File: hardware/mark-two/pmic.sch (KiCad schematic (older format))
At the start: 30 parts, among them U1 MC34PF1510A6EP

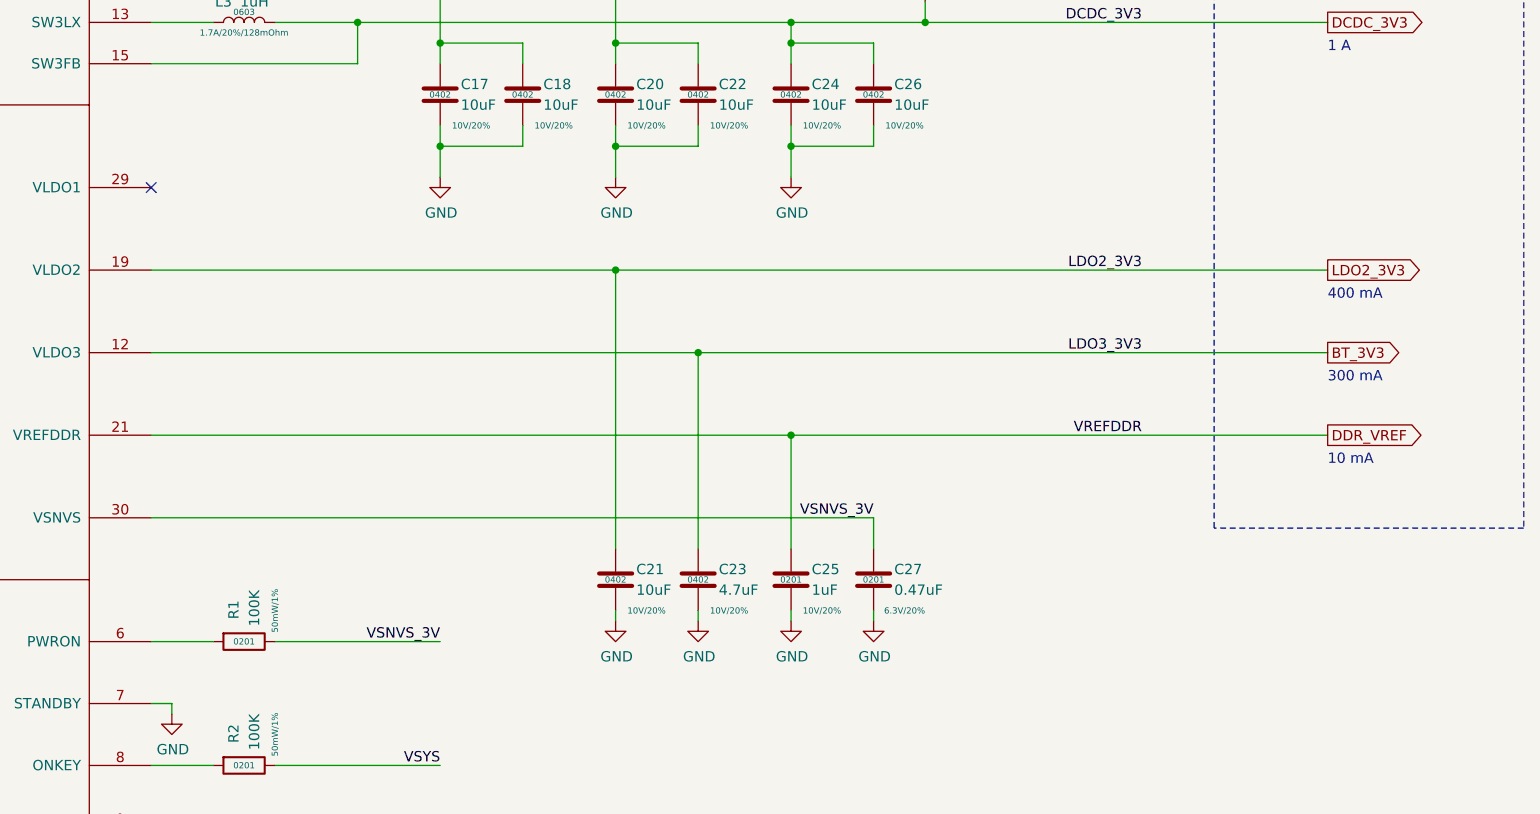
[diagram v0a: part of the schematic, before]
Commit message: add USB armory Mk II rev. γ
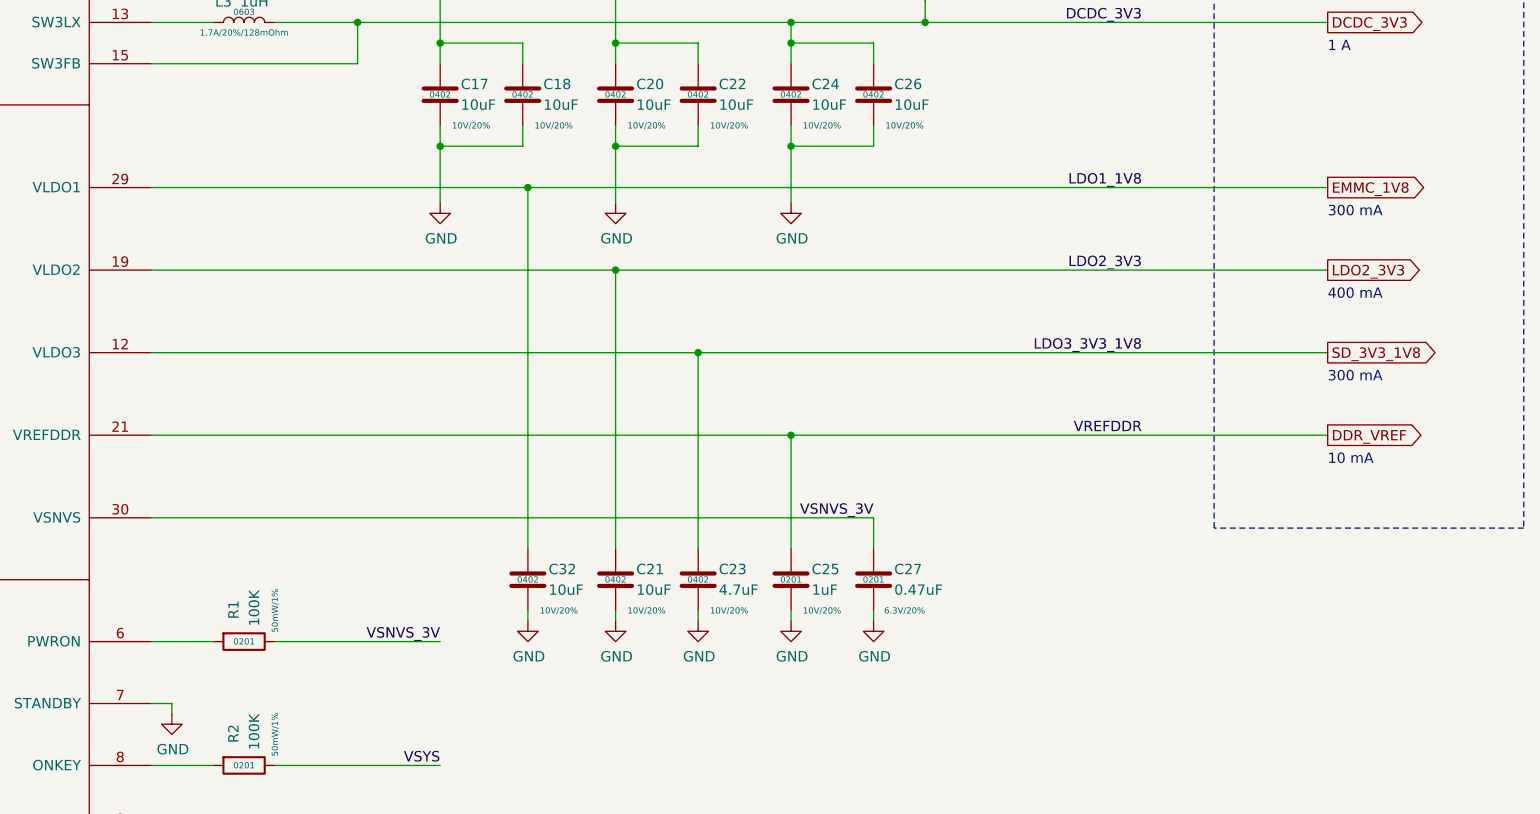
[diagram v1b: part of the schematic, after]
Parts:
- added C32: 10uF, armory-kicad:SM0402, symbol Device:C
- C10, C14, C15, C25, C4, C8, C9: Alternative PN (none) -> CL03A105KP3NSNC
- C13: Alternative PN (none) -> GRT155R61E225KE13D
- C16: Alternative PN (none) -> 06036D476MAT2A
- U1: Alternative PN (none) -> MC32PF1510A6EP
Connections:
- net GND: now also C32.2
- net EMMC_1V8: now reaches U1.29 (VLDO1)
- net EMMC_1V8: now also C32.1
- net BT_3V3 renamed SD_3V3_1V8
- no-connect marks 7 -> 6
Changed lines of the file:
@@
 EESchema Schematic File Version 4
-LIBS:armory-cache
 EELAYER 30 0
 EELAYER END
@@
 encoding utf-8
 Sheet 13 13
-Title "USB ARMORY"
-Date "2019-06-25"
-Rev "MARK II"
+Title "USB armory Mk II"
+Date "2021-02-18"
+Rev "γ"
 Comp "F-Secure"
-Comment1 "Copyright © 2019 F-Secure"
-Comment2 "License: CERN OHL v1.2"
-Comment3 "https://github.com/inversepath/usbarmory"
+Comment1 "Copyright © F-Secure Corporation"
+Comment2 "License: CERN-OHL-S"
+Comment3 "https://github.com/f-secure-foundry/usbarmory"
 Comment4 ""
 $EndDescr
@@
 LDO2_3V3
 Text Label 13150 5000 2    50   ~ 0
-LDO3_3V3
+LDO3_3V3_1V8
 $Comp
 L power:GND #PWR?
@@
 L power:GND #PWR?
 U 1 1 5C23D7E7
-P 9750 4150
+P 9750 4275
 AR Path="/5BEA6694/5C23D7E7" Ref="#PWR?"  Part="1"
 AR Path="/53722D05/5C23D7E7" Ref="#PWR?"  Part="1"
@@
 AR Path="/5C6BBC6A/5C23D7E7" Ref="#PWR?"  Part="1"
 AR Path="/5D0EEC79/5C23D7E7" Ref="#PWR?"  Part="1"
-F 0 "#PWR016" H 9750 3900 50  0001 C CNN
-F 1 "GND" H 9755 3977 50  0000 C CNN
-F 2 "" H 9750 4150 50  0001 C CNN
-F 3 "" H 9750 4150 50  0001 C CNN
-	1    9750 4150
+F 0 "#PWR016" H 9750 4025 50  0001 C CNN
+F 1 "GND" H 9755 4102 50  0000 C CNN
+F 2 "" H 9750 4275 50  0001 C CNN
+F 3 "" H 9750 4275 50  0001 C CNN
+	1    9750 4275
 	1    0    0    -1
 $EndComp
@@
 Connection ~ 9750 4000
 Wire Wire Line
-	9750 4000 9750 4150
+	9750 4000 9750 4275
 $Comp
 L power:GND #PWR?
 U 1 1 5C2BD78A
-P 10600 4150
+P 10600 4275
 AR Path="/5BEA6694/5C2BD78A" Ref="#PWR?"  Part="1"
 AR Path="/53722D05/5C2BD78A" Ref="#PWR?"  Part="1"
@@
 AR Path="/5C6BBC6A/5C2BD78A" Ref="#PWR?"  Part="1"
 AR Path="/5D0EEC79/5C2BD78A" Ref="#PWR?"  Part="1"
-F 0 "#PWR018" H 10600 3900 50  0001 C CNN
-F 1 "GND" H 10605 3977 50  0000 C CNN
-F 2 "" H 10600 4150 50  0001 C CNN
-F 3 "" H 10600 4150 50  0001 C CNN
-	1    10600 4150
+F 0 "#PWR018" H 10600 4025 50  0001 C CNN
+F 1 "GND" H 10605 4102 50  0000 C CNN
+F 2 "" H 10600 4275 50  0001 C CNN
+F 3 "" H 10600 4275 50  0001 C CNN
+	1    10600 4275
 	1    0    0    -1
 $EndComp
@@
 Connection ~ 10600 4000
 Wire Wire Line
-	10600 4000 10600 4150
+	10600 4000 10600 4275
 Wire Wire Line
 	10600 3600 10600 3500
@@
 L power:GND #PWR?
 U 1 1 5C2FA4BD
-P 11450 4150
+P 11450 4275
 AR Path="/5BEA6694/5C2FA4BD" Ref="#PWR?"  Part="1"
 AR Path="/53722D05/5C2FA4BD" Ref="#PWR?"  Part="1"
@@
 AR Path="/5C6BBC6A/5C2FA4BD" Ref="#PWR?"  Part="1"
 AR Path="/5D0EEC79/5C2FA4BD" Ref="#PWR?"  Part="1"
-F 0 "#PWR021" H 11450 3900 50  0001 C CNN
-F 1 "GND" H 11455 3977 50  0000 C CNN
-F 2 "" H 11450 4150 50  0001 C CNN
-F 3 "" H 11450 4150 50  0001 C CNN
-	1    11450 4150
+F 0 "#PWR021" H 11450 4025 50  0001 C CNN
+F 1 "GND" H 11455 4102 50  0000 C CNN
+F 2 "" H 11450 4275 50  0001 C CNN
+F 3 "" H 11450 4275 50  0001 C CNN
+	1    11450 4275
 	1    0    0    -1
 $EndComp
@@
 Connection ~ 11450 4000
 Wire Wire Line
-	11450 4000 11450 4150
+	11450 4000 11450 4275
 Wire Wire Line
 	11450 3600 11450 3500
@@
 LDO2_3V3
 Text GLabel 14050 5000 2    50   Output ~ 0
-BT_3V3
+SD_3V3_1V8
 Text GLabel 4550 7200 0    50   Input ~ 0
 I2C1_SCL
@@
 F 7 "Digikey" H 7100 1000 50  0001 C CNN "Supplier"
 F 8 "568-14653-1-ND" H 7100 1000 50  0001 C CNN "Supplier PN"
+F 9 "MC32PF1510A6EP" H 7100 1000 50  0001 C CNN "Alternative PN"
 	1    7100 1000
 	1    0    0    -1
@@
 Wire Wire Line
 	11000 5000 11000 5950
-NoConn ~ 8350 4200
 Text Label 9750 7000 2    50   ~ 0
 VSYS
@@
 Text Label 9750 6400 2    50   ~ 0
 VSNVS_3V
-Wire Wire Line
-	10600 5950 10600 4600
 Wire Wire Line
 	8350 4600 10600 4600
@@
 F 9 "0201" H 1900 4550 30  0000 C CNN "FP"
 F 10 "10V/20%" H 2050 4400 30  0000 C CNN "Rating"
+F 11 "CL03A105KP3NSNC" H 1900 4550 50  0001 C CNN "Alternative PN"
 	1    1900 4550
 	1    0    0    -1
@@
 F 9 "0201" H 2350 4550 30  0000 C CNN "FP"
 F 10 "10V/20%" H 2500 4400 30  0000 C CNN "Rating"
+F 11 "CL03A105KP3NSNC" H 2350 4550 50  0001 C CNN "Alternative PN"
 	1    2350 4550
 	1    0    0    -1
@@
 F 9 "0201" H 2800 4550 30  0000 C CNN "FP"
 F 10 "10V/20%" H 2950 4400 30  0000 C CNN "Rating"
+F 11 "CL03A105KP3NSNC" H 2800 4550 50  0001 C CNN "Alternative PN"
 	1    2800 4550
 	1    0    0    -1
@@
 F 9 "0201" H 5200 9050 30  0000 C CNN "FP"
 F 10 "10V/20%" H 5350 8900 30  0000 C CNN "Rating"
+F 11 "CL03A105KP3NSNC" H 5200 9050 50  0001 C CNN "Alternative PN"
 	1    5200 9050
 	1    0    0    -1
@@
 F 9 "0201" H 5650 9050 30  0000 C CNN "FP"
 F 10 "10V/20%" H 5800 8900 30  0000 C CNN "Rating"
+F 11 "CL03A105KP3NSNC" H 5650 9050 50  0001 C CNN "Alternative PN"
 	1    5650 9050
 	1    0    0    -1
@@
 F 9 "0201" H 11450 6100 30  0000 C CNN "FP"
 F 10 "10V/20%" H 11600 5950 30  0000 C CNN "Rating"
+F 11 "CL03A105KP3NSNC" H 11450 6100 50  0001 C CNN "Alternative PN"
 	1    11450 6100
 	1    0    0    -1
@@
 F 9 "0402" H 5200 1450 30  0000 C CNN "FP"
 F 10 "25V/20%" H 5350 1300 30  0000 C CNN "Rating"
+F 11 "GRT155R61E225KE13D" H 5200 1450 50  0001 C CNN "Alternative PN"
 	1    5200 1450
 	1    0    0    -1
@@
 F 9 "0603" H 9750 1450 30  0000 C CNN "FP"
 F 10 "6.3V/20%" H 9900 1300 30  0000 C CNN "Rating"
+F 11 "06036D476MAT2A" H 9750 1450 50  0001 C CNN "Alternative PN"
 	1    9750 1450
 	1    0    0    -1
@@
 F 9 "0201" H 4250 6000 30  0000 C CNN "FP"
 F 10 "10V/20%" H 4400 5850 30  0000 C CNN "Rating"
+F 11 "CL03A105KP3NSNC" H 4250 6000 50  0001 C CNN "Alternative PN"
 	1    4250 6000
 	1    0    0    -1
@@
 Text Notes 5725 10000 0    100  ~ 0
 ULL/ULZ: NXP MC34PF1510A6EP\n      UL: NXP MC32PF1510A3EP
+Wire Wire Line
+	10600 5950 10600 4600
+Text GLabel 14050 4200 2    50   Output ~ 0
+EMMC_1V8
+Text Notes 14050 4350 0    50   ~ 0
+300 mA
+$Comp
+L power:GND #PWR?
+U 1 1 5F1896E1
+P 10175 6300
+AR Path="/5BEA6694/5F1896E1" Ref="#PWR?"  Part="1"
+AR Path="/53722D05/5F1896E1" Ref="#PWR?"  Part="1"
+AR Path="/5335DA0B/5F1896E1" Ref="#PWR0130"  Part="1"
+AR Path="/5C6BBC6A/5F1896E1" Ref="#PWR?"  Part="1"
+AR Path="/5D0EEC79/5F1896E1" Ref="#PWR?"  Part="1"
+F 0 "#PWR0130" H 10175 6050 50  0001 C CNN
+F 1 "GND" H 10180 6127 50  0000 C CNN
+F 2 "" H 10175 6300 50  0001 C CNN
+F 3 "" H 10175 6300 50  0001 C CNN
+	1    10175 6300
+	1    0    0    -1
+$EndComp
+Wire Wire Line
+	10175 6250 10175 6300
+$Comp
+L Device:C C?
+U 1 1 5F1896F3
+P 10175 6100
+AR Path="/5BEA6694/5F1896F3" Ref="C?"  Part="1"
+AR Path="/5335DA0B/5F1896F3" Ref="C32"  Part="1"
+AR Path="/53722D05/5F1896F3" Ref="C?"  Part="1"
+AR Path="/5D0EEC79/5F1896F3" Ref="C?"  Part="1"
+F 0 "C32" H 10275 6150 50  0000 L CNN
+F 1 "10uF" H 10275 6050 50  0000 L CNN
+F 2 "armory-kicad:SM0402" H 10213 5950 50  0001 C CNN
+F 3 "~" H 10175 6100 50  0001 C CNN
+F 4 "Samsung Electro-Mechanics" H 10175 6100 50  0001 C CNN "Mfg"
+F 5 "CL05A106MP8NUB8" H 10175 6100 50  0001 C CNN "Mfg PN"
+F 6 "X5R, 20%, 10V" H 10175 6100 50  0001 C CNN "Desc"
+F 7 "Digikey" H 10175 6100 50  0001 C CNN "Supplier"
+F 8 "1276-6830-1-ND" H 10175 6100 50  0001 C CNN "Supplier PN"
+F 9 "0402" H 10175 6100 30  0000 C CNN "FP"
+F 10 "10V/20%" H 10325 5950 30  0000 C CNN "Rating"
+	1    10175 6100
+	1    0    0    -1
+$EndComp
+Wire Wire Line
+	10175 5950 10175 4200
+Wire Wire Line
+	8350 4200 10175 4200
+Text Label 13150 4200 2    50   ~ 0
+LDO1_1V8
+Connection ~ 10175 4200
+Wire Wire Line
+	10175 4200 14050 4200
 $EndSCHEMATC
